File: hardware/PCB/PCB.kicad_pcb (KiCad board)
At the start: 2 copper layers, 81.5 x 55.1 mm, 14 parts, among them J1 Header, J2 Conn_01x02, J3 Conn_01x01_Male, U1 GAL16V8, U2 74LVC245A, U3 74LVC245A

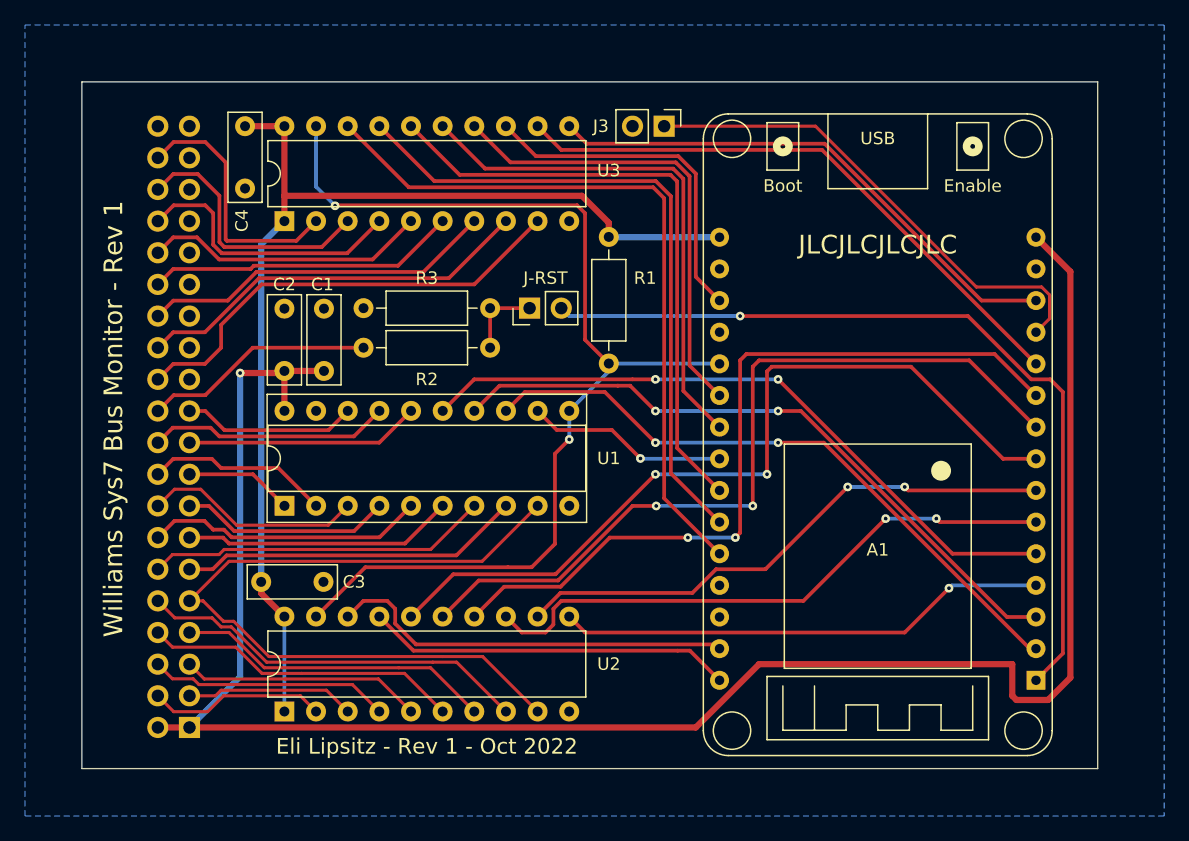
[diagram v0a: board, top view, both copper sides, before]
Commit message: pcb: create rev2, using raspberry pi pico w
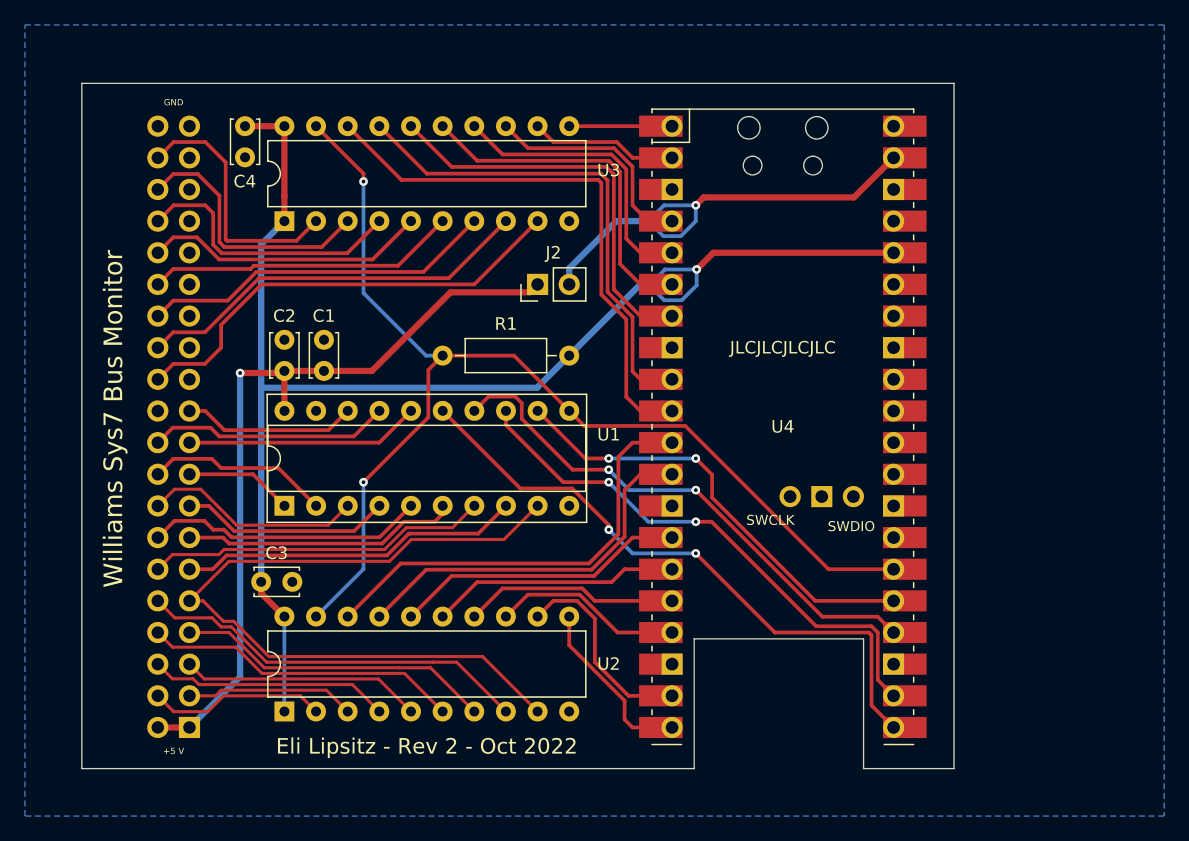
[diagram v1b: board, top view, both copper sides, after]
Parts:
- removed A1: ESP32-DEV-30, footprint-library:esp32_devkit_v1_doit
- removed J3: Conn_01x01_Male, Connector_PinHeader_2.54mm:PinHeader_1x02_P2.54mm_Vertical
- removed R2: 4k7, Resistor_THT:R_Axial_DIN0207_L6.3mm_D2.5mm_P10.16mm_Horizontal
- removed R3: 10k, Resistor_THT:R_Axial_DIN0207_L6.3mm_D2.5mm_P10.16mm_Horizontal
- added U4: Pico, MCU_RaspberryPi_and_Boards:RPi_PicoW_SMD_TH, F.Cu at (101.0, 92.7)
- C1, C2, C3, C4: footprint Capacitor_THT:C_Disc_D7.0mm_W2.5mm_P5.00mm -> Capacitor_THT:C_Disc_D3.4mm_W2.1mm_P2.50mm
- moved R1 10.0 mm to (83.8, 87.0), turned to 180 degrees
- moved J2 2.01 mm to (81.3, 81.3)
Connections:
- J2 pad 1: /3V-~{RESET} -> +5V
- J2 pad 2: /ESP32-~{RESET} -> Net-(J2-Pad2)
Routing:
- net +5V: track 155.4 -> 62.7 mm
- net /ESP32-~{RESET}: track 67.1 -> 0.00 mm, vias 1 -> 0
- net /3V-A4: track 63.3 -> 17.2 mm, vias 2 -> 0
- net /3V-A3: track 64.9 -> 20.0 mm, vias 2 -> 0
- net /3V-A2: track 66.4 -> 23.6 mm, vias 2 -> 0
- net Net-(A1-Pad12): track 40.0 -> 0.00 mm
- net Net-(J2-Pad2): track 0.00 -> 37.1 mm, vias 0 -> 1
- net /3V-D1: track 47.9 -> 11.8 mm
- net /3V-D0: track 43.3 -> 8.26 mm
- net /3V-A5: track 47.7 -> 15.3 mm, vias 2 -> 0
- net /3V-A6: track 44.5 -> 16.5 mm, vias 2 -> 0
- net /3V-A7: track 39.6 -> 14.2 mm, vias 1 -> 0
- net +3.3V: track 88.5 -> 112.9 mm, vias 0 -> 1
- net /3V-WREN: track 16.2 -> 36.0 mm, vias 1 -> 2
- net /3V-D5: track 49.4 -> 30.1 mm
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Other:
- board size 81.5 x 55.1 mm -> 70 x 55 mm
- board text added: "+5 V"
- board text added: "Eli Lipsitz - Rev 2 - Oct 2022"
- board text added: "GND"
- board text added: "Williams Sys7 Bus Monitor"
- board text removed: "Eli Lipsitz - Rev 1 - Oct 2022"
- board text removed: "J-RST"
- board text removed: "Williams Sys7 Bus Monitor - Rev 1"

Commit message: Finish PCB rev2
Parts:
- removed J2: Conn_01x02, Connector_PinHeader_2.54mm:PinHeader_1x02_P2.54mm_Vertical
- added D1: 1N5819, Diode_THT:D_DO-41_SOD81_P10.16mm_Horizontal, F.Cu at (83.8, 83.2)
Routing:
- net +5V: track 62.7 -> 54.3 mm
- net Net-(U4-Pad39): track 37.1 -> 39.0 mm
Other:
- board text added: "Eli Lipsitz - Rev 2 - Nov 2022"
- board text removed: "Eli Lipsitz - Rev 2 - Oct 2022"
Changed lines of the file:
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@@
       (psa4output false)
       (plotreference true)
-      (plotvalue true)
+      (plotvalue false)
       (plotinvisibletext false)
       (sketchpadsonfab false)
@@
   (net 71 "unconnected-(U4-Pad41)")
   (net 72 "unconnected-(U4-Pad43)")
-  (net 73 "Net-(J2-Pad2)")
+  (net 73 "Net-(U4-Pad39)")
   (footprint "MCU_RaspberryPi_and_Boards:RPi_PicoW_SMD_TH" (layer "F.Cu")
     (at 100.965 92.71)
@@
       (net 14 "GND") (pinfunction "GND") (pintype "power_in"))
     (pad "39" smd rect (at 8.89 -21.59) (size 3.5 1.7) (drill (offset 0.9 0)) (layers "F.Cu" "F.Mask")
-      (net 73 "Net-(J2-Pad2)") (pinfunction "VSYS") (pintype "power_in"))
+      (net 73 "Net-(U4-Pad39)") (pinfunction "VSYS") (pintype "power_in"))
     (pad "39" thru_hole oval (at 8.89 -21.59) (size 1.7 1.7) (drill 1.02) (layers *.Cu *.Mask)
-      (net 73 "Net-(J2-Pad2)") (pinfunction "VSYS") (pintype "power_in"))
+      (net 73 "Net-(U4-Pad39)") (pinfunction "VSYS") (pintype "power_in"))
     (pad "40" smd rect (at 8.89 -24.13) (size 3.5 1.7) (drill (offset 0.9 0)) (layers "F.Cu" "F.Mask")
       (net 70 "unconnected-(U4-Pad40)") (pinfunction "VBUS") (pintype "input+no_connect"))
@@
     )
   )
-  (footprint "Connector_PinHeader_2.54mm:PinHeader_1x02_P2.54mm_Vertical" (layer "F.Cu")
-    (at 81.28 81.28 90)
-    (descr "Through hole straight pin header, 1x02, 2.54mm pitch, single row")
-    (tags "Through hole pin header THT 1x02 2.54mm single row")
+  (footprint "Diode_THT:D_DO-41_SOD81_P10.16mm_Horizontal" (layer "F.Cu")
+    (at 83.82 83.185 180)
+    (descr "Diode, DO-41_SOD81 series, Axial, Horizontal, pin pitch=10.16mm, , length*diameter=5.2*2.7mm^2, , http://www.diodes.com/_files/packages/DO-41%20(Plastic).pdf")
+    (tags "Diode DO-41_SOD81 series Axial Horizontal pin pitch 10.16mm  length 5.2mm diameter 2.7mm")
     (property "Sheetfile" "File: PCB.kicad_sch")
     (property "Sheetname" "")
     (attr through_hole)
-    (fp_text reference "J2" (at 2.54 1.27 180) (layer "F.SilkS")
-      (effects (font (size 1 1) (thickness 0.15)))
-    )
-    (fp_text value "Conn_01x02" (at 0 4.87 90) (layer "F.Fab")
-      (effects (font (size 1 1) (thickness 0.15)))
-    )
-    (fp_text user "${REFERENCE}" (at 0 1.27) (layer "F.Fab")
-      (effects (font (size 1 1) (thickness 0.15)))
-    )
-    (fp_line (start -1.33 1.27) (end -1.33 3.87) (layer "F.SilkS") (width 0.12))
-    (fp_line (start -1.33 -1.33) (end 0 -1.33) (layer "F.SilkS") (width 0.12))
-    (fp_line (start -1.33 0) (end -1.33 -1.33) (layer "F.SilkS") (width 0.12))
-    (fp_line (start 1.33 1.27) (end 1.33 3.87) (layer "F.SilkS") (width 0.12))
-    (fp_line (start -1.33 1.27) (end 1.33 1.27) (layer "F.SilkS") (width 0.12))
-    (fp_line (start -1.33 3.87) (end 1.33 3.87) (layer "F.SilkS") (width 0.12))
-    (fp_line (start 1.8 -1.8) (end -1.8 -1.8) (layer "F.CrtYd") (width 0.05))
-    (fp_line (start -1.8 4.35) (end 1.8 4.35) (layer "F.CrtYd") (width 0.05))
-    (fp_line (start 1.8 4.35) (end 1.8 -1.8) (layer "F.CrtYd") (width 0.05))
-    (fp_line (start -1.8 -1.8) (end -1.8 4.35) (layer "F.CrtYd") (width 0.05))
-    (fp_line (start 1.27 -1.27) (end 1.27 3.81) (layer "F.Fab") (width 0.1))
-    (fp_line (start -1.27 3.81) (end -1.27 -0.635) (layer "F.Fab") (width 0.1))
-    (fp_line (start -1.27 -0.635) (end -0.635 -1.27) (layer "F.Fab") (width 0.1))
-    (fp_line (start -0.635 -1.27) (end 1.27 -1.27) (layer "F.Fab") (width 0.1))
-    (fp_line (start 1.27 3.81) (end -1.27 3.81) (layer "F.Fab") (width 0.1))
-    (pad "1" thru_hole rect (at 0 0 90) (size 1.7 1.7) (drill 1) (layers *.Cu *.Mask)
-      (net 15 "+5V") (pinfunction "Pin_1") (pintype "passive"))
-    (pad "2" thru_hole oval (at 0 2.54 90) (size 1.7 1.7) (drill 1) (layers *.Cu *.Mask)
-      (net 73 "Net-(J2-Pad2)") (pinfunction "Pin_2") (pintype "passive"))
-    (model "${KICAD6_3DMODEL_DIR}/Connector_PinHeader_2.54mm.3dshapes/PinHeader_1x02_P2.54mm_Vertical.wrl"
+    (fp_text reference "D1" (at -2.54 0) (layer "F.SilkS")
+      (effects (font (size 1 1) (thickness 0.15)))
+    )
+    (fp_text value "1N5819" (at 5.08 2.47) (layer "F.Fab")
+      (effects (font (size 1 1) (thickness 0.15)))
+    )
+    (fp_text user "K" (at 0 2.54) (layer "F.SilkS")
+      (effects (font (size 1 1) (thickness 0.15)))
+    )
+    (fp_text user "K" (at 0 -2.1) (layer "F.Fab")
+      (effects (font (size 1 1) (thickness 0.15)))
+    )
+    (fp_text user "${REFERENCE}" (at 5.47 0) (layer "F.Fab")
+      (effects (font (size 1 1) (thickness 0.15)))
+    )
+    (fp_line (start 2.36 -1.47) (end 2.36 1.47) (layer "F.SilkS") (width 0.12))
+    (fp_line (start 8.82 0) (end 7.8 0) (layer "F.SilkS") (width 0.12))
+    (fp_line (start 1.34 0) (end 2.36 0) (layer "F.SilkS") (width 0.12))
+    (fp_line (start 3.26 -1.47) (end 3.26 1.47) (layer "F.SilkS") (width 0.12))
+    (fp_line (start 2.36 1.47) (end 7.8 1.47) (layer "F.SilkS") (width 0.12))
+    (fp_line (start 7.8 1.47) (end 7.8 -1.47) (layer "F.SilkS") (width 0.12))
+    (fp_line (start 3.14 -1.47) (end 3.14 1.47) (layer "F.SilkS") (width 0.12))
+    (fp_line (start 3.38 -1.47) (end 3.38 1.47) (layer "F.SilkS") (width 0.12))
+    (fp_line (start 7.8 -1.47) (end 2.36 -1.47) (layer "F.SilkS") (width 0.12))
+    (fp_line (start 11.51 -1.6) (end -1.35 -1.6) (layer "F.CrtYd") (width 0.05))
+    (fp_line (start 11.51 1.6) (end 11.51 -1.6) (layer "F.CrtYd") (width 0.05))
+    (fp_line (start -1.35 1.6) (end 11.51 1.6) (layer "F.CrtYd") (width 0.05))
+    (fp_line (start -1.35 -1.6) (end -1.35 1.6) (layer "F.CrtYd") (width 0.05))
+    (fp_line (start 7.68 -1.35) (end 2.48 -1.35) (layer "F.Fab") (width 0.1))
+    (fp_line (start 2.48 1.35) (end 7.68 1.35) (layer "F.Fab") (width 0.1))
+    (fp_line (start 3.16 -1.35) (end 3.16 1.35) (layer "F.Fab") (width 0.1))
+    (fp_line (start 3.26 -1.35) (end 3.26 1.35) (layer "F.Fab") (width 0.1))
+    (fp_line (start 7.68 1.35) (end 7.68 -1.35) (layer "F.Fab") (width 0.1))
+    (fp_line (start 3.36 -1.35) (end 3.36 1.35) (layer "F.Fab") (width 0.1))
+    (fp_line (start 10.16 0) (end 7.68 0) (layer "F.Fab") (width 0.1))
+    (fp_line (start 2.48 -1.35) (end 2.48 1.35) (layer "F.Fab") (width 0.1))
+    (fp_line (start 0 0) (end 2.48 0) (layer "F.Fab") (width 0.1))
+    (pad "1" thru_hole rect (at 0 0 180) (size 2.2 2.2) (drill 1.1) (layers *.Cu *.Mask)
+      (net 73 "Net-(U4-Pad39)") (pinfunction "K") (pintype "passive"))
+    (pad "2" thru_hole oval (at 10.16 0 180) (size 2.2 2.2) (drill 1.1) (layers *.Cu *.Mask)
+      (net 15 "+5V") (pinfunction "A") (pintype "passive"))
+    (model "${KICAD6_3DMODEL_DIR}/Diode_THT.3dshapes/D_DO-41_SOD81_P10.16mm_Horizontal.wrl"
       (offset (xyz 0 0 0))
       (scale (xyz 1 1 1))
@@
     (property "Sheetname" "")
     (attr through_hole)
-    (fp_text reference "R1" (at 5.08 2.54 180) (layer "F.SilkS")
+    (fp_text reference "R1" (at -2.54 0 180) (layer "F.SilkS")
       (effects (font (size 1 1) (thickness 0.15)))
     )
@@
     (effects (font (size 0.5 0.5) (thickness 0.1)))
   )
-  (gr_text "Eli Lipsitz - Rev 2 - Oct 2022" (at 72.39 118.364) (layer "F.SilkS")
+  (gr_text "Eli Lipsitz - Rev 2 - Nov 2022" (at 72.39 118.364) (layer "F.SilkS")
     (effects (font (size 1.25 1.25) (thickness 0.2)))
   )
@@
   (segment (start 83.82 68.58) (end 92.075 68.58) (width 0.3) (layer "F.Cu") (net 13))
   (segment (start 60.96 88.225) (end 64.135 88.225) (width 0.5) (layer "F.Cu") (net 15))
-  (segment (start 64.135 88.225) (end 67.985 88.225) (width 0.5) (layer "F.Cu") (net 15))
   (segment (start 60.793 88.392) (end 60.96 88.225) (width 0.5) (layer "F.Cu") (net 15))
   (segment (start 57.404 88.392) (end 60.793 88.392) (width 0.5) (layer "F.Cu") (net 15))
   (segment (start 60.96 88.225) (end 60.96 91.425) (width 0.5) (layer "F.Cu") (net 15))
-  (segment (start 67.985 88.225) (end 74.295 81.915) (width 0.5) (layer "F.Cu") (net 15))
   (segment (start 60.96 91.425) (end 60.965 91.43) (width 0.5) (layer "F.Cu") (net 15))
   (segment (start 50.8 116.84) (end 53.34 116.84) (width 0.5) (layer "F.Cu") (net 15))
-  (segment (start 74.295 81.915) (end 80.645 81.915) (width 0.5) (layer "F.Cu") (net 15))
-  (segment (start 80.645 81.915) (end 81.28 81.28) (width 0.5) (layer "F.Cu") (net 15))
+  (segment (start 64.135 88.225) (end 68.62 88.225) (width 0.5) (layer "F.Cu") (net 15))
+  (segment (start 68.62 88.225) (end 73.66 83.185) (width 0.5) (layer "F.Cu") (net 15))
   (via (at 57.404 88.392) (size 0.7) (drill 0.3) (layers "F.Cu" "B.Cu") (net 15))
   (segment (start 57.404 112.776) (end 57.404 88.392) (width 0.5) (layer "B.Cu") (net 15))
@@
   (segment (start 92.78 77.4) (end 93.345 76.835) (width 0.3) (layer "B.Cu") (net 73))
   (segment (start 93.345 76.835) (end 93.98 76.2) (width 0.3) (layer "B.Cu") (net 73))
-  (segment (start 87.6055 76.2) (end 90.17 76.2) (width 0.5) (layer "B.Cu") (net 73))
   (segment (start 93.98 76.2) (end 93.98 74.93) (width 0.3) (layer "B.Cu") (net 73))
-  (segment (start 83.82 81.28) (end 83.82 79.9855) (width 0.5) (layer "B.Cu") (net 73))
-  (segment (start 83.82 79.9855) (end 87.6055 76.2) (width 0.5) (layer "B.Cu") (net 73))
+  (segment (start 87.6055 76.2) (end 83.82 79.9855) (width 0.5) (layer "B.Cu") (net 73))
   (segment (start 91.37 77.4) (end 92.78 77.4) (width 0.3) (layer "B.Cu") (net 73))
+  (segment (start 83.82 79.9855) (end 83.82 83.185) (width 0.5) (layer "B.Cu") (net 73))
+  (segment (start 90.17 76.2) (end 87.6055 76.2) (width 0.5) (layer "B.Cu") (net 73))
   (segment (start 90.17 76.2) (end 91.37 77.4) (width 0.3) (layer "B.Cu") (net 73))
   (segment (start 91.44 74.93) (end 93.98 74.93) (width 0.3) (layer "B.Cu") (net 73))
